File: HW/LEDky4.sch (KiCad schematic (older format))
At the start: 8 parts

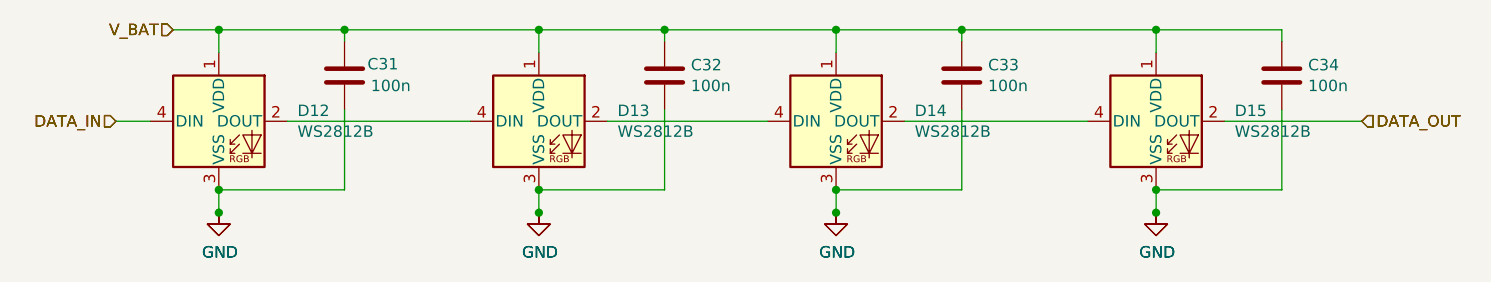
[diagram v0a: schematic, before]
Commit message: repair WS2812B na WS2812C
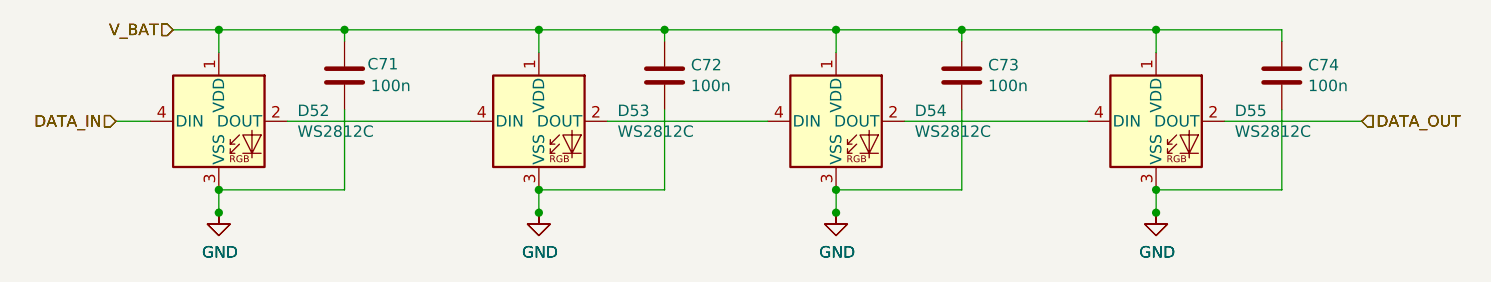
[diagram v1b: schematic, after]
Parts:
- D56, D57, D58, D59: value WS2812B -> WS2812C
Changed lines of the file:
@@
 $Descr A4 11693 8268
 encoding utf-8
-Sheet 7 28
+Sheet 19 28
 Title ""
 Date ""
@@
 AR Path="/5F79BCD0/5FB77CB0/5F78FD5C" Ref="#PWR0122"  Part="1"
 AR Path="/5FACC290/5FB77CB0/5F78FD5C" Ref="#PWR0207"  Part="1"
-F 0 "#PWR050" H 3700 3850 50  0001 C CNN
+F 0 "#PWR0135" H 3700 3850 50  0001 C CNN
 F 1 "GND" H 3705 3927 50  0000 C CNN
 F 2 "" H 3700 4100 50  0001 C CNN
@@
 AR Path="/5F79BCD0/5FB77CB0/5F78FD62" Ref="C67"  Part="1"
 AR Path="/5FACC290/5FB77CB0/5F78FD62" Ref="C107"  Part="1"
-F 0 "C31" H 4350 3550 50  0000 L CNN
+F 0 "C71" H 4350 3550 50  0000 L CNN
 F 1 "100n" H 4365 3455 50  0000 L CNN
 F 2 "Capacitor_SMD:C_0402_1005Metric" H 4288 3350 50  0001 C CNN
@@
 AR Path="/5F79BCD0/5FB77CB0/5F78FD71" Ref="D49"  Part="1"
 AR Path="/5FACC290/5FB77CB0/5F78FD71" Ref="D89"  Part="1"
-F 0 "D13" H 5444 3746 50  0000 L CNN
-F 1 "WS2812B" H 5444 3655 50  0000 L CNN
+F 0 "D53" H 5444 3746 50  0000 L CNN
+F 1 "WS2812C" H 5444 3655 50  0000 L CNN
 F 2 "LED_SMD:LED_WS2812B_PLCC4_5.0x5.0mm_P3.2mm" H 5150 3400 50  0001 L TNN
 F 3 "https://cdn-shop.adafruit.com/datasheets/WS2812B.pdf" H 5200 3325 50  0001 L TNN
@@
 AR Path="/5F79BCD0/5FB77CB0/5F798BEB" Ref="#PWR0125"  Part="1"
 AR Path="/5FACC290/5FB77CB0/5F798BEB" Ref="#PWR0210"  Part="1"
-F 0 "#PWR053" H 5100 3850 50  0001 C CNN
+F 0 "#PWR0138" H 5100 3850 50  0001 C CNN
 F 1 "GND" H 5105 3927 50  0000 C CNN
 F 2 "" H 5100 4100 50  0001 C CNN
@@
 AR Path="/5F79BCD0/5FB77CB0/5F798BEE" Ref="#PWR0127"  Part="1"
 AR Path="/5FACC290/5FB77CB0/5F798BEE" Ref="#PWR0212"  Part="1"
-F 0 "#PWR055" H 6400 3850 50  0001 C CNN
+F 0 "#PWR0140" H 6400 3850 50  0001 C CNN
 F 1 "GND" H 6405 3927 50  0000 C CNN
 F 2 "" H 6400 4100 50  0001 C CNN
@@
 AR Path="/5F79BCD0/5FB77CB0/5F78FDA5" Ref="D51"  Part="1"
 AR Path="/5FACC290/5FB77CB0/5F78FDA5" Ref="D91"  Part="1"
-F 0 "D15" H 8144 3746 50  0000 L CNN
-F 1 "WS2812B" H 8144 3655 50  0000 L CNN
+F 0 "D55" H 8144 3746 50  0000 L CNN
+F 1 "WS2812C" H 8144 3655 50  0000 L CNN
 F 2 "LED_SMD:LED_WS2812B_PLCC4_5.0x5.0mm_P3.2mm" H 7850 3400 50  0001 L TNN
 F 3 "https://cdn-shop.adafruit.com/datasheets/WS2812B.pdf" H 7900 3325 50  0001 L TNN
@@
 AR Path="/5F79BCD0/5FB77CB0/5F78FDAB" Ref="#PWR0128"  Part="1"
 AR Path="/5FACC290/5FB77CB0/5F78FDAB" Ref="#PWR0213"  Part="1"
-F 0 "#PWR056" H 7800 3850 50  0001 C CNN
+F 0 "#PWR0141" H 7800 3850 50  0001 C CNN
 F 1 "GND" H 7805 3927 50  0000 C CNN
 F 2 "" H 7800 4100 50  0001 C CNN
@@
 AR Path="/5F79BCD0/5FB77CB0/5F78FDB1" Ref="C70"  Part="1"
 AR Path="/5FACC290/5FB77CB0/5F78FDB1" Ref="C110"  Part="1"
-F 0 "C34" H 8465 3546 50  0000 L CNN
+F 0 "C74" H 8465 3546 50  0000 L CNN
 F 1 "100n" H 8465 3455 50  0000 L CNN
 F 2 "Capacitor_SMD:C_0402_1005Metric" H 8388 3350 50  0001 C CNN
@@
 AR Path="/5F79BCD0/5FB77CB0/5F78FD56" Ref="D48"  Part="1"
 AR Path="/5FACC290/5FB77CB0/5F78FD56" Ref="D88"  Part="1"
-F 0 "D12" H 4044 3746 50  0000 L CNN
-F 1 "WS2812B" H 4044 3655 50  0000 L CNN
+F 0 "D52" H 4044 3746 50  0000 L CNN
+F 1 "WS2812C" H 4044 3655 50  0000 L CNN
 F 2 "LED_SMD:LED_WS2812B_PLCC4_5.0x5.0mm_P3.2mm" H 3750 3400 50  0001 L TNN
 F 3 "https://cdn-shop.adafruit.com/datasheets/WS2812B.pdf" H 3800 3325 50  0001 L TNN
@@
 AR Path="/5F79BCD0/5FB77CB0/5F798BE8" Ref="#PWR0123"  Part="1"
 AR Path="/5FACC290/5FB77CB0/5F798BE8" Ref="#PWR0208"  Part="1"
-F 0 "#PWR051" H 3700 3850 50  0001 C CNN
+F 0 "#PWR0136" H 3700 3850 50  0001 C CNN
 F 1 "GND" H 3705 3927 50  0000 C CNN
 F 2 "" H 3700 4100 50  0001 C CNN
@@
 AR Path="/5F79BCD0/5FB77CB0/5F78FD77" Ref="#PWR0124"  Part="1"
 AR Path="/5FACC290/5FB77CB0/5F78FD77" Ref="#PWR0209"  Part="1"
-F 0 "#PWR052" H 5100 3850 50  0001 C CNN
+F 0 "#PWR0137" H 5100 3850 50  0001 C CNN
 F 1 "GND" H 5105 3927 50  0000 C CNN
 F 2 "" H 5100 4100 50  0001 C CNN
@@
 AR Path="/5F79BCD0/5FB77CB0/5F78FD7D" Ref="C68"  Part="1"
 AR Path="/5FACC290/5FB77CB0/5F78FD7D" Ref="C108"  Part="1"
-F 0 "C32" H 5765 3546 50  0000 L CNN
+F 0 "C72" H 5765 3546 50  0000 L CNN
 F 1 "100n" H 5765 3455 50  0000 L CNN
 F 2 "Capacitor_SMD:C_0402_1005Metric" H 5688 3350 50  0001 C CNN
@@
 AR Path="/5F79BCD0/5FB77CB0/5F78FD8B" Ref="D50"  Part="1"
 AR Path="/5FACC290/5FB77CB0/5F78FD8B" Ref="D90"  Part="1"
-F 0 "D14" H 6744 3746 50  0000 L CNN
-F 1 "WS2812B" H 6744 3655 50  0000 L CNN
+F 0 "D54" H 6744 3746 50  0000 L CNN
+F 1 "WS2812C" H 6744 3655 50  0000 L CNN
 F 2 "LED_SMD:LED_WS2812B_PLCC4_5.0x5.0mm_P3.2mm" H 6450 3400 50  0001 L TNN
 F 3 "https://cdn-shop.adafruit.com/datasheets/WS2812B.pdf" H 6500 3325 50  0001 L TNN
@@
 AR Path="/5F79BCD0/5FB77CB0/5F78FD91" Ref="#PWR0126"  Part="1"
 AR Path="/5FACC290/5FB77CB0/5F78FD91" Ref="#PWR0211"  Part="1"
-F 0 "#PWR054" H 6400 3850 50  0001 C CNN
+F 0 "#PWR0139" H 6400 3850 50  0001 C CNN
 F 1 "GND" H 6405 3927 50  0000 C CNN
 F 2 "" H 6400 4100 50  0001 C CNN
@@
 AR Path="/5F79BCD0/5FB77CB0/5F78FD97" Ref="C69"  Part="1"
 AR Path="/5FACC290/5FB77CB0/5F78FD97" Ref="C109"  Part="1"
-F 0 "C33" H 7065 3546 50  0000 L CNN
+F 0 "C73" H 7065 3546 50  0000 L CNN
 F 1 "100n" H 7065 3455 50  0000 L CNN
 F 2 "Capacitor_SMD:C_0402_1005Metric" H 6988 3350 50  0001 C CNN
@@
 AR Path="/5F79BCD0/5FB77CB0/5F798BF1" Ref="#PWR0129"  Part="1"
 AR Path="/5FACC290/5FB77CB0/5F798BF1" Ref="#PWR0214"  Part="1"
-F 0 "#PWR057" H 7800 3850 50  0001 C CNN
+F 0 "#PWR0142" H 7800 3850 50  0001 C CNN
 F 1 "GND" H 7805 3927 50  0000 C CNN
 F 2 "" H 7800 4100 50  0001 C CNN

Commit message: V1.1 change SMD buttons, add diode on VCC
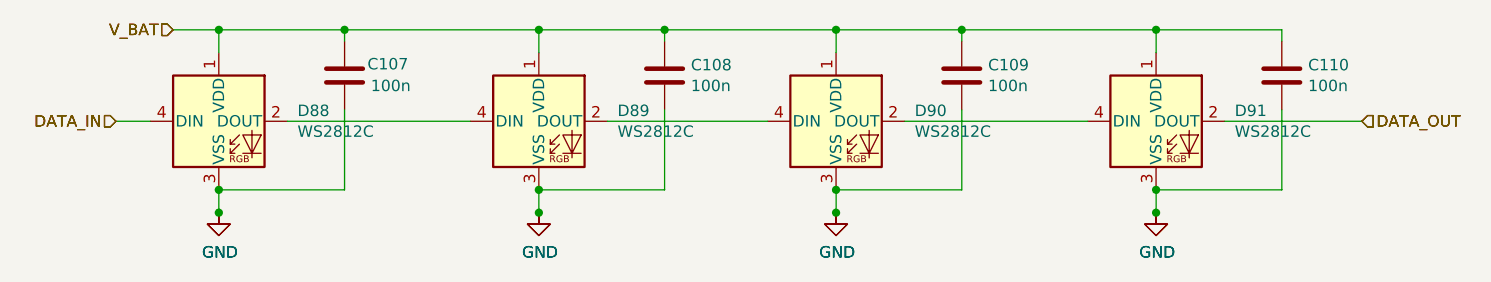
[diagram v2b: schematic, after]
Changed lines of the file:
@@
 AR Path="/5F79BCD0/5FB77CB0/5F78FD5C" Ref="#PWR0122"  Part="1"
 AR Path="/5FACC290/5FB77CB0/5F78FD5C" Ref="#PWR0207"  Part="1"
-F 0 "#PWR0135" H 3700 3850 50  0001 C CNN
+F 0 "#PWR0207" H 3700 3850 50  0001 C CNN
 F 1 "GND" H 3705 3927 50  0000 C CNN
 F 2 "" H 3700 4100 50  0001 C CNN
@@
 AR Path="/5F79BCD0/5FB77CB0/5F78FD62" Ref="C67"  Part="1"
 AR Path="/5FACC290/5FB77CB0/5F78FD62" Ref="C107"  Part="1"
-F 0 "C71" H 4350 3550 50  0000 L CNN
+F 0 "C107" H 4350 3550 50  0000 L CNN
 F 1 "100n" H 4365 3455 50  0000 L CNN
 F 2 "Capacitor_SMD:C_0402_1005Metric" H 4288 3350 50  0001 C CNN
@@
 AR Path="/5F79BCD0/5FB77CB0/5F78FD71" Ref="D49"  Part="1"
 AR Path="/5FACC290/5FB77CB0/5F78FD71" Ref="D89"  Part="1"
-F 0 "D53" H 5444 3746 50  0000 L CNN
+F 0 "D89" H 5444 3746 50  0000 L CNN
 F 1 "WS2812C" H 5444 3655 50  0000 L CNN
 F 2 "LED_SMD:LED_WS2812B_PLCC4_5.0x5.0mm_P3.2mm" H 5150 3400 50  0001 L TNN
@@
 AR Path="/5F79BCD0/5FB77CB0/5F798BEB" Ref="#PWR0125"  Part="1"
 AR Path="/5FACC290/5FB77CB0/5F798BEB" Ref="#PWR0210"  Part="1"
-F 0 "#PWR0138" H 5100 3850 50  0001 C CNN
+F 0 "#PWR0210" H 5100 3850 50  0001 C CNN
 F 1 "GND" H 5105 3927 50  0000 C CNN
 F 2 "" H 5100 4100 50  0001 C CNN
@@
 AR Path="/5F79BCD0/5FB77CB0/5F798BEE" Ref="#PWR0127"  Part="1"
 AR Path="/5FACC290/5FB77CB0/5F798BEE" Ref="#PWR0212"  Part="1"
-F 0 "#PWR0140" H 6400 3850 50  0001 C CNN
+F 0 "#PWR0212" H 6400 3850 50  0001 C CNN
 F 1 "GND" H 6405 3927 50  0000 C CNN
 F 2 "" H 6400 4100 50  0001 C CNN
@@
 AR Path="/5F79BCD0/5FB77CB0/5F78FDA5" Ref="D51"  Part="1"
 AR Path="/5FACC290/5FB77CB0/5F78FDA5" Ref="D91"  Part="1"
-F 0 "D55" H 8144 3746 50  0000 L CNN
+F 0 "D91" H 8144 3746 50  0000 L CNN
 F 1 "WS2812C" H 8144 3655 50  0000 L CNN
 F 2 "LED_SMD:LED_WS2812B_PLCC4_5.0x5.0mm_P3.2mm" H 7850 3400 50  0001 L TNN
@@
 AR Path="/5F79BCD0/5FB77CB0/5F78FDAB" Ref="#PWR0128"  Part="1"
 AR Path="/5FACC290/5FB77CB0/5F78FDAB" Ref="#PWR0213"  Part="1"
-F 0 "#PWR0141" H 7800 3850 50  0001 C CNN
+F 0 "#PWR0213" H 7800 3850 50  0001 C CNN
 F 1 "GND" H 7805 3927 50  0000 C CNN
 F 2 "" H 7800 4100 50  0001 C CNN
@@
 AR Path="/5F79BCD0/5FB77CB0/5F78FDB1" Ref="C70"  Part="1"
 AR Path="/5FACC290/5FB77CB0/5F78FDB1" Ref="C110"  Part="1"
-F 0 "C74" H 8465 3546 50  0000 L CNN
+F 0 "C110" H 8465 3546 50  0000 L CNN
 F 1 "100n" H 8465 3455 50  0000 L CNN
 F 2 "Capacitor_SMD:C_0402_1005Metric" H 8388 3350 50  0001 C CNN
@@
 AR Path="/5F79BCD0/5FB77CB0/5F78FD56" Ref="D48"  Part="1"
 AR Path="/5FACC290/5FB77CB0/5F78FD56" Ref="D88"  Part="1"
-F 0 "D52" H 4044 3746 50  0000 L CNN
+F 0 "D88" H 4044 3746 50  0000 L CNN
 F 1 "WS2812C" H 4044 3655 50  0000 L CNN
 F 2 "LED_SMD:LED_WS2812B_PLCC4_5.0x5.0mm_P3.2mm" H 3750 3400 50  0001 L TNN
@@
 AR Path="/5F79BCD0/5FB77CB0/5F798BE8" Ref="#PWR0123"  Part="1"
 AR Path="/5FACC290/5FB77CB0/5F798BE8" Ref="#PWR0208"  Part="1"
-F 0 "#PWR0136" H 3700 3850 50  0001 C CNN
+F 0 "#PWR0208" H 3700 3850 50  0001 C CNN
 F 1 "GND" H 3705 3927 50  0000 C CNN
 F 2 "" H 3700 4100 50  0001 C CNN
@@
 AR Path="/5F79BCD0/5FB77CB0/5F78FD77" Ref="#PWR0124"  Part="1"
 AR Path="/5FACC290/5FB77CB0/5F78FD77" Ref="#PWR0209"  Part="1"
-F 0 "#PWR0137" H 5100 3850 50  0001 C CNN
+F 0 "#PWR0209" H 5100 3850 50  0001 C CNN
 F 1 "GND" H 5105 3927 50  0000 C CNN
 F 2 "" H 5100 4100 50  0001 C CNN
@@
 AR Path="/5F79BCD0/5FB77CB0/5F78FD7D" Ref="C68"  Part="1"
 AR Path="/5FACC290/5FB77CB0/5F78FD7D" Ref="C108"  Part="1"
-F 0 "C72" H 5765 3546 50  0000 L CNN
+F 0 "C108" H 5765 3546 50  0000 L CNN
 F 1 "100n" H 5765 3455 50  0000 L CNN
 F 2 "Capacitor_SMD:C_0402_1005Metric" H 5688 3350 50  0001 C CNN
@@
 AR Path="/5F79BCD0/5FB77CB0/5F78FD8B" Ref="D50"  Part="1"
 AR Path="/5FACC290/5FB77CB0/5F78FD8B" Ref="D90"  Part="1"
-F 0 "D54" H 6744 3746 50  0000 L CNN
+F 0 "D90" H 6744 3746 50  0000 L CNN
 F 1 "WS2812C" H 6744 3655 50  0000 L CNN
 F 2 "LED_SMD:LED_WS2812B_PLCC4_5.0x5.0mm_P3.2mm" H 6450 3400 50  0001 L TNN
@@
 AR Path="/5F79BCD0/5FB77CB0/5F78FD91" Ref="#PWR0126"  Part="1"
 AR Path="/5FACC290/5FB77CB0/5F78FD91" Ref="#PWR0211"  Part="1"
-F 0 "#PWR0139" H 6400 3850 50  0001 C CNN
+F 0 "#PWR0211" H 6400 3850 50  0001 C CNN
 F 1 "GND" H 6405 3927 50  0000 C CNN
 F 2 "" H 6400 4100 50  0001 C CNN
@@
 AR Path="/5F79BCD0/5FB77CB0/5F78FD97" Ref="C69"  Part="1"
 AR Path="/5FACC290/5FB77CB0/5F78FD97" Ref="C109"  Part="1"
-F 0 "C73" H 7065 3546 50  0000 L CNN
+F 0 "C109" H 7065 3546 50  0000 L CNN
 F 1 "100n" H 7065 3455 50  0000 L CNN
 F 2 "Capacitor_SMD:C_0402_1005Metric" H 6988 3350 50  0001 C CNN
@@
 AR Path="/5F79BCD0/5FB77CB0/5F798BF1" Ref="#PWR0129"  Part="1"
 AR Path="/5FACC290/5FB77CB0/5F798BF1" Ref="#PWR0214"  Part="1"
-F 0 "#PWR0142" H 7800 3850 50  0001 C CNN
+F 0 "#PWR0214" H 7800 3850 50  0001 C CNN
 F 1 "GND" H 7805 3927 50  0000 C CNN
 F 2 "" H 7800 4100 50  0001 C CNN

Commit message: repair footprint of DIP and USB micro, change buttons with higher fretboard
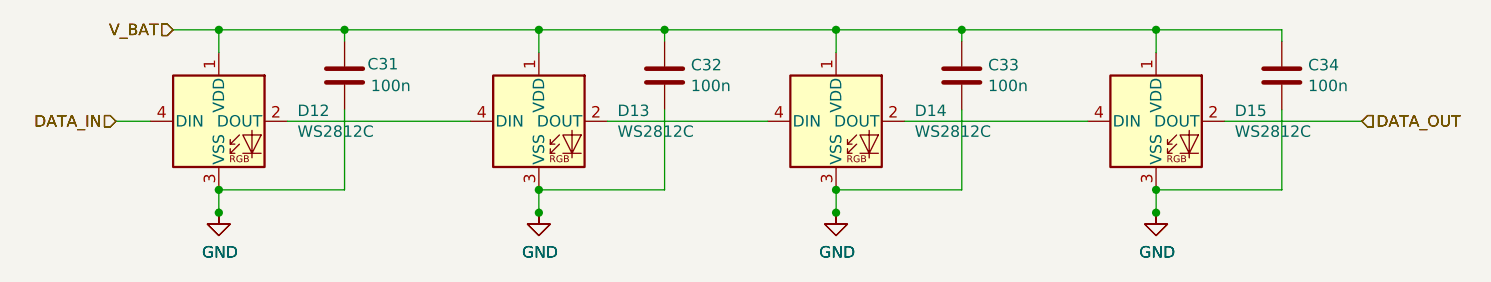
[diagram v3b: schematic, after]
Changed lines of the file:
@@
 $Descr A4 11693 8268
 encoding utf-8
-Sheet 19 28
+Sheet 7 28
 Title ""
 Date ""
@@
 AR Path="/5F79BCD0/5FB77CB0/5F78FD62" Ref="C67"  Part="1"
 AR Path="/5FACC290/5FB77CB0/5F78FD62" Ref="C107"  Part="1"
-F 0 "C107" H 4350 3550 50  0000 L CNN
+F 0 "C31" H 4350 3550 50  0000 L CNN
 F 1 "100n" H 4365 3455 50  0000 L CNN
 F 2 "Capacitor_SMD:C_0402_1005Metric" H 4288 3350 50  0001 C CNN
@@
 AR Path="/5F79BCD0/5FB77CB0/5F78FD71" Ref="D49"  Part="1"
 AR Path="/5FACC290/5FB77CB0/5F78FD71" Ref="D89"  Part="1"
-F 0 "D89" H 5444 3746 50  0000 L CNN
+F 0 "D13" H 5444 3746 50  0000 L CNN
 F 1 "WS2812C" H 5444 3655 50  0000 L CNN
 F 2 "LED_SMD:LED_WS2812B_PLCC4_5.0x5.0mm_P3.2mm" H 5150 3400 50  0001 L TNN
@@
 AR Path="/5F79BCD0/5FB77CB0/5F78FDA5" Ref="D51"  Part="1"
 AR Path="/5FACC290/5FB77CB0/5F78FDA5" Ref="D91"  Part="1"
-F 0 "D91" H 8144 3746 50  0000 L CNN
+F 0 "D15" H 8144 3746 50  0000 L CNN
 F 1 "WS2812C" H 8144 3655 50  0000 L CNN
 F 2 "LED_SMD:LED_WS2812B_PLCC4_5.0x5.0mm_P3.2mm" H 7850 3400 50  0001 L TNN
@@
 AR Path="/5F79BCD0/5FB77CB0/5F78FDB1" Ref="C70"  Part="1"
 AR Path="/5FACC290/5FB77CB0/5F78FDB1" Ref="C110"  Part="1"
-F 0 "C110" H 8465 3546 50  0000 L CNN
+F 0 "C34" H 8465 3546 50  0000 L CNN
 F 1 "100n" H 8465 3455 50  0000 L CNN
 F 2 "Capacitor_SMD:C_0402_1005Metric" H 8388 3350 50  0001 C CNN
@@
 AR Path="/5F79BCD0/5FB77CB0/5F78FD56" Ref="D48"  Part="1"
 AR Path="/5FACC290/5FB77CB0/5F78FD56" Ref="D88"  Part="1"
-F 0 "D88" H 4044 3746 50  0000 L CNN
+F 0 "D12" H 4044 3746 50  0000 L CNN
 F 1 "WS2812C" H 4044 3655 50  0000 L CNN
 F 2 "LED_SMD:LED_WS2812B_PLCC4_5.0x5.0mm_P3.2mm" H 3750 3400 50  0001 L TNN
@@
 AR Path="/5F79BCD0/5FB77CB0/5F78FD7D" Ref="C68"  Part="1"
 AR Path="/5FACC290/5FB77CB0/5F78FD7D" Ref="C108"  Part="1"
-F 0 "C108" H 5765 3546 50  0000 L CNN
+F 0 "C32" H 5765 3546 50  0000 L CNN
 F 1 "100n" H 5765 3455 50  0000 L CNN
 F 2 "Capacitor_SMD:C_0402_1005Metric" H 5688 3350 50  0001 C CNN
@@
 AR Path="/5F79BCD0/5FB77CB0/5F78FD8B" Ref="D50"  Part="1"
 AR Path="/5FACC290/5FB77CB0/5F78FD8B" Ref="D90"  Part="1"
-F 0 "D90" H 6744 3746 50  0000 L CNN
+F 0 "D14" H 6744 3746 50  0000 L CNN
 F 1 "WS2812C" H 6744 3655 50  0000 L CNN
 F 2 "LED_SMD:LED_WS2812B_PLCC4_5.0x5.0mm_P3.2mm" H 6450 3400 50  0001 L TNN
@@
 AR Path="/5F79BCD0/5FB77CB0/5F78FD97" Ref="C69"  Part="1"
 AR Path="/5FACC290/5FB77CB0/5F78FD97" Ref="C109"  Part="1"
-F 0 "C109" H 7065 3546 50  0000 L CNN
+F 0 "C33" H 7065 3546 50  0000 L CNN
 F 1 "100n" H 7065 3455 50  0000 L CNN
 F 2 "Capacitor_SMD:C_0402_1005Metric" H 6988 3350 50  0001 C CNN

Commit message: change USB footprint, add 3. DIP
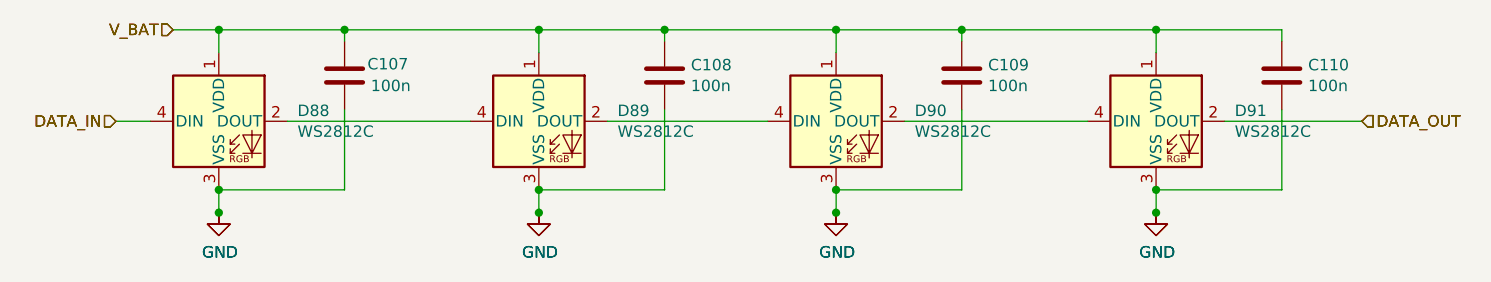
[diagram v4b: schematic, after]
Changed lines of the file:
@@
 AR Path="/5F79BCD0/5FB77CB0/5F78FD62" Ref="C67"  Part="1"
 AR Path="/5FACC290/5FB77CB0/5F78FD62" Ref="C107"  Part="1"
-F 0 "C31" H 4350 3550 50  0000 L CNN
+F 0 "C107" H 4350 3550 50  0000 L CNN
 F 1 "100n" H 4365 3455 50  0000 L CNN
 F 2 "Capacitor_SMD:C_0402_1005Metric" H 4288 3350 50  0001 C CNN
@@
 AR Path="/5F79BCD0/5FB77CB0/5F78FD71" Ref="D49"  Part="1"
 AR Path="/5FACC290/5FB77CB0/5F78FD71" Ref="D89"  Part="1"
-F 0 "D13" H 5444 3746 50  0000 L CNN
+F 0 "D89" H 5444 3746 50  0000 L CNN
 F 1 "WS2812C" H 5444 3655 50  0000 L CNN
 F 2 "LED_SMD:LED_WS2812B_PLCC4_5.0x5.0mm_P3.2mm" H 5150 3400 50  0001 L TNN
@@
 AR Path="/5F79BCD0/5FB77CB0/5F78FDA5" Ref="D51"  Part="1"
 AR Path="/5FACC290/5FB77CB0/5F78FDA5" Ref="D91"  Part="1"
-F 0 "D15" H 8144 3746 50  0000 L CNN
+F 0 "D91" H 8144 3746 50  0000 L CNN
 F 1 "WS2812C" H 8144 3655 50  0000 L CNN
 F 2 "LED_SMD:LED_WS2812B_PLCC4_5.0x5.0mm_P3.2mm" H 7850 3400 50  0001 L TNN
@@
 AR Path="/5F79BCD0/5FB77CB0/5F78FDB1" Ref="C70"  Part="1"
 AR Path="/5FACC290/5FB77CB0/5F78FDB1" Ref="C110"  Part="1"
-F 0 "C34" H 8465 3546 50  0000 L CNN
+F 0 "C110" H 8465 3546 50  0000 L CNN
 F 1 "100n" H 8465 3455 50  0000 L CNN
 F 2 "Capacitor_SMD:C_0402_1005Metric" H 8388 3350 50  0001 C CNN
@@
 AR Path="/5F79BCD0/5FB77CB0/5F78FD56" Ref="D48"  Part="1"
 AR Path="/5FACC290/5FB77CB0/5F78FD56" Ref="D88"  Part="1"
-F 0 "D12" H 4044 3746 50  0000 L CNN
+F 0 "D88" H 4044 3746 50  0000 L CNN
 F 1 "WS2812C" H 4044 3655 50  0000 L CNN
 F 2 "LED_SMD:LED_WS2812B_PLCC4_5.0x5.0mm_P3.2mm" H 3750 3400 50  0001 L TNN
@@
 AR Path="/5F79BCD0/5FB77CB0/5F78FD7D" Ref="C68"  Part="1"
 AR Path="/5FACC290/5FB77CB0/5F78FD7D" Ref="C108"  Part="1"
-F 0 "C32" H 5765 3546 50  0000 L CNN
+F 0 "C108" H 5765 3546 50  0000 L CNN
 F 1 "100n" H 5765 3455 50  0000 L CNN
 F 2 "Capacitor_SMD:C_0402_1005Metric" H 5688 3350 50  0001 C CNN
@@
 AR Path="/5F79BCD0/5FB77CB0/5F78FD8B" Ref="D50"  Part="1"
 AR Path="/5FACC290/5FB77CB0/5F78FD8B" Ref="D90"  Part="1"
-F 0 "D14" H 6744 3746 50  0000 L CNN
+F 0 "D90" H 6744 3746 50  0000 L CNN
 F 1 "WS2812C" H 6744 3655 50  0000 L CNN
 F 2 "LED_SMD:LED_WS2812B_PLCC4_5.0x5.0mm_P3.2mm" H 6450 3400 50  0001 L TNN
@@
 AR Path="/5F79BCD0/5FB77CB0/5F78FD97" Ref="C69"  Part="1"
 AR Path="/5FACC290/5FB77CB0/5F78FD97" Ref="C109"  Part="1"
-F 0 "C33" H 7065 3546 50  0000 L CNN
+F 0 "C109" H 7065 3546 50  0000 L CNN
 F 1 "100n" H 7065 3455 50  0000 L CNN
 F 2 "Capacitor_SMD:C_0402_1005Metric" H 6988 3350 50  0001 C CNN

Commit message: update rotation of components for fab, update folder fab
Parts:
- D56, D57, D58, D59: JLCPCB_CORRECTION 0;0;90 -> 0;0;180
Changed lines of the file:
@@
 F 3 "https://cdn-shop.adafruit.com/datasheets/WS2812B.pdf" H 5200 3325 50  0001 L TNN
 F 4 "C114587" H 5100 3700 50  0001 C CNN "LCSC"
-F 5 "0;0;90" H 5100 3700 50  0001 C CNN "JLCPCB_CORRECTION"
+F 5 "0;0;180" H 5100 3700 50  0001 C CNN "JLCPCB_CORRECTION"
 	1    5100 3700
 	1    0    0    -1
@@
 F 3 "https://cdn-shop.adafruit.com/datasheets/WS2812B.pdf" H 7900 3325 50  0001 L TNN
 F 4 "C114587" H 7800 3700 50  0001 C CNN "LCSC"
-F 5 "0;0;90" H 7800 3700 50  0001 C CNN "JLCPCB_CORRECTION"
+F 5 "0;0;180" H 7800 3700 50  0001 C CNN "JLCPCB_CORRECTION"
 	1    7800 3700
 	1    0    0    -1
@@
 F 3 "https://cdn-shop.adafruit.com/datasheets/WS2812B.pdf" H 3800 3325 50  0001 L TNN
 F 4 "C114587" H 3700 3700 50  0001 C CNN "LCSC"
-F 5 "0;0;90" H 3700 3700 50  0001 C CNN "JLCPCB_CORRECTION"
+F 5 "0;0;180" H 3700 3700 50  0001 C CNN "JLCPCB_CORRECTION"
 	1    3700 3700
 	1    0    0    -1
@@
 F 3 "https://cdn-shop.adafruit.com/datasheets/WS2812B.pdf" H 6500 3325 50  0001 L TNN
 F 4 "C114587" H 6400 3700 50  0001 C CNN "LCSC"
-F 5 "0;0;90" H 6400 3700 50  0001 C CNN "JLCPCB_CORRECTION"
+F 5 "0;0;180" H 6400 3700 50  0001 C CNN "JLCPCB_CORRECTION"
 	1    6400 3700
 	1    0    0    -1
